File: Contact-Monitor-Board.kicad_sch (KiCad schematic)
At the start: 82 parts, among them J1 JST VH 02, J10 JST VH 02, J11 JST VH 02, J12 JST VH 02, J13 JST VH 02, J14 JST VH 02, J15 JST VH 02, J16 JST VH 02, J17 header 4, J2 JST VH 02, J3 JST VH 02, J4 JST VH 02, J5 JST VH 02, J6 JST VH 02, J7 JST VH 02, J8 JST VH 02, J9 JST VH 02, Q1 2N7002, Q10 2N7002, Q11 2N7002, Q12 2N7002, Q13 2N7002, Q14 2N7002, Q15 2N7002, Q16 2N7002, Q2 2N7002, Q3 2N7002, Q4 2N7002, Q5 2N7002, Q6 2N7002, Q7 2N7002, Q8 2N7002, Q9 2N7002, SW1 KH-SS12D01-G3-5.0, U1 74HC4017D, U2 TLC555CD, U3 TPS61222DCK

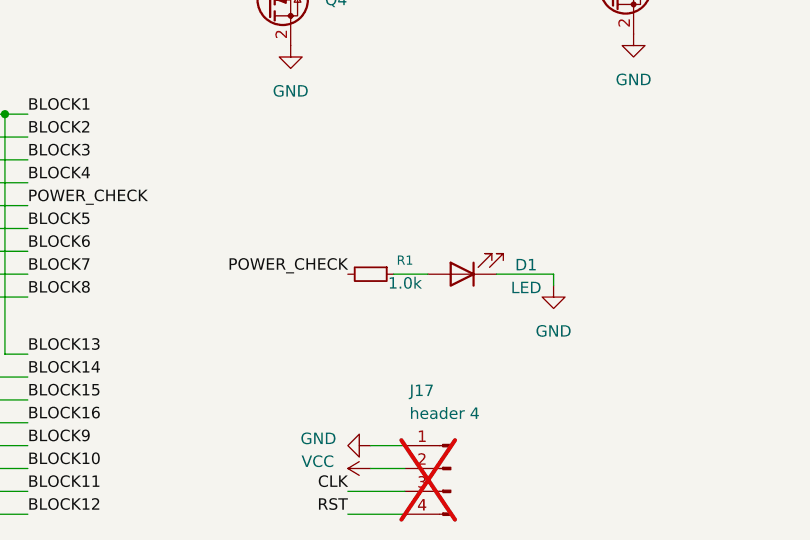
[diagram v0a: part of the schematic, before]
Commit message: V1.3.1 電池ケース裏面のランド追加とシルク・寸法注記の整備
- BT1 のスルーホールパッドを "*.Cu" "*.Mask" に変更し、裏面にランドと
  マスク開口を追加（従来は F.Mask のみで裏面が露出していなかった）。
  THT なので F.Paste は削除。ライブラリと基板の双方を更新
- 運転 LED の輝度を再調整し R1 を 470 に戻す。README の
  「抵抗は 470 Ω と 4.7 kΩ の 2 種類」の構成と整合させる
- タイトルシルクを knockout 化し、下線をドットに変更
- 取付穴 4-φ5.2 と外形寸法の注記を Cmts.User に追加
- rev を 1.3.1 に更新し、ガーバー / BOM / CPL / PDF を再生成
- 基板レンダリング画像（表・裏）を追加

DRC: 違反 0 / 未配線 0 / 回路図パリティ 0

Co-Authored-By: Claude Opus 5 <noreply@anthropic.com>
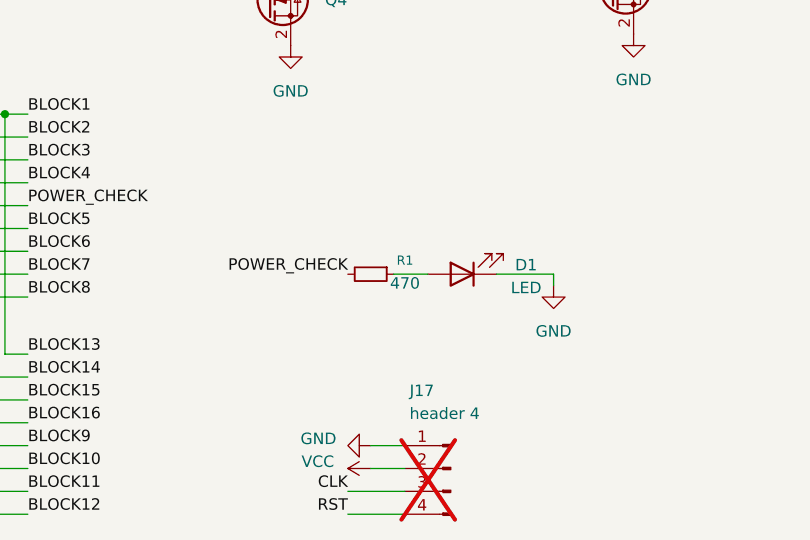
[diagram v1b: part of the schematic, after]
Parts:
- R1: value 1.0k -> 470
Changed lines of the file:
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@@
 	(title_block
 		(title "Contact Monitor Board")
-		(date "2026-08-13")
-		(rev "1.3")
+		(date "2026-08-19")
+		(rev "1.3.1")
 		(company "Satoru Yamaguchi")
 		(comment 1 "Copyright (c) 2026 Satoru Yamaguchi")
@@
 			)
 		)
-		(property "Value" "1.0k"
+		(property "Value" "470"
 			(at 156.21 153.416 90)
 			(effects
